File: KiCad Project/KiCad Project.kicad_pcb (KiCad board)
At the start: 4 copper layers, 69 parts, among them J1 XT30PW-M, J2 USB_C_Receptacle_USB2.0_16P, J3 PYRO, J4 PYRO ARM, J5 SWD, J6 Micro_SD_Card, Q1 GSFC02A05, Q2 FDMC7692, U1 STM32F103C8T6, U2 ICM-42670-P, U3 BME280, U4 AT25SF041B-SSHD-T, U5 PESD3V3S4UD,115, U6 AP63203WU, U7 ESD122DMXR, U8 AZ1117CH2-3.3, U9 ESD122DMXR, Y1 ECS-2520MV-160-CN-TR

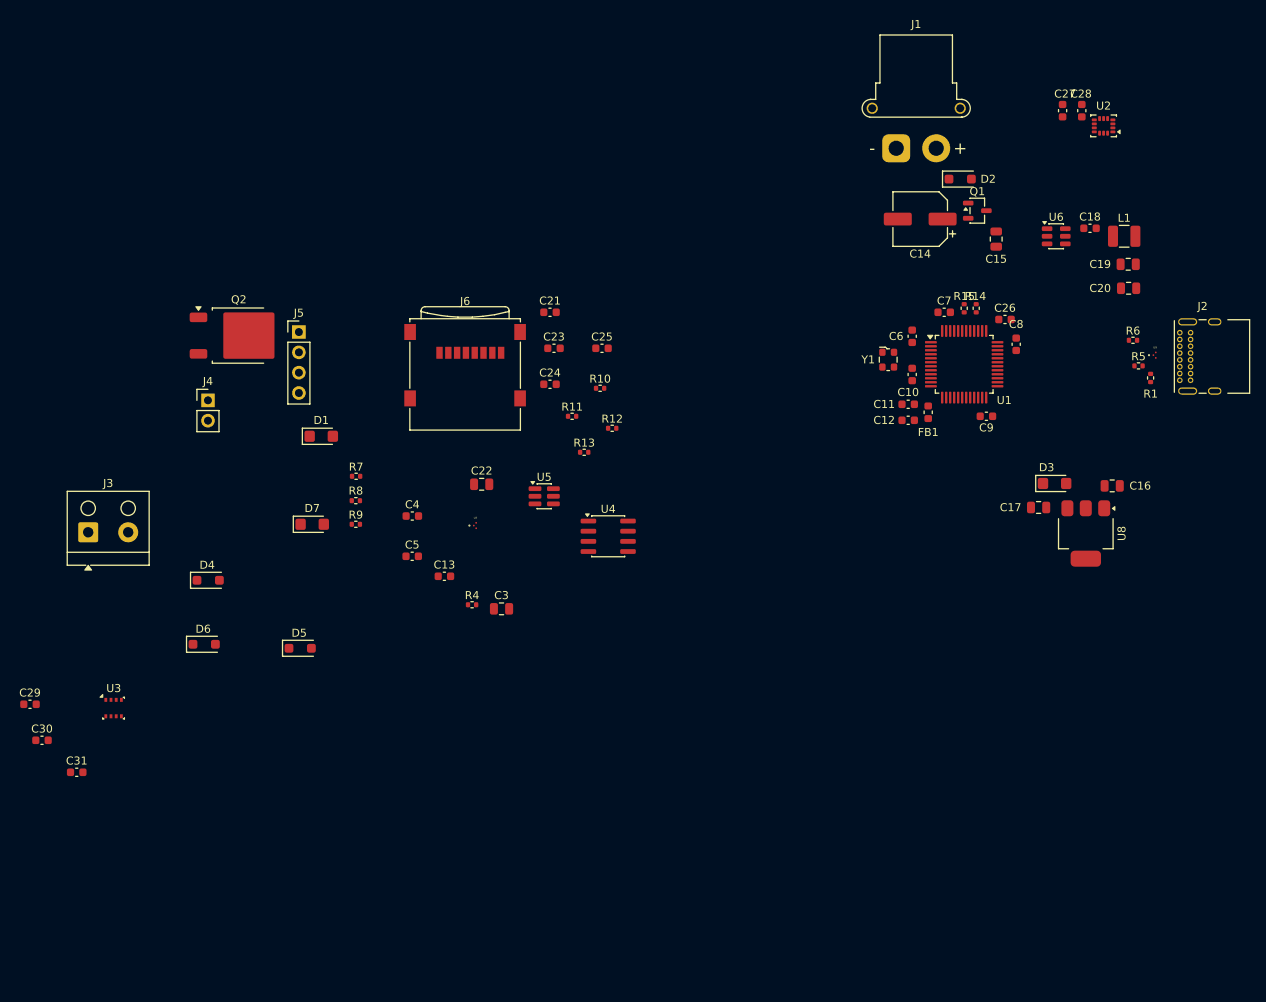
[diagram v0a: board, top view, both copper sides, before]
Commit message: Updated layout, documentation and schematic. Component placement finished.
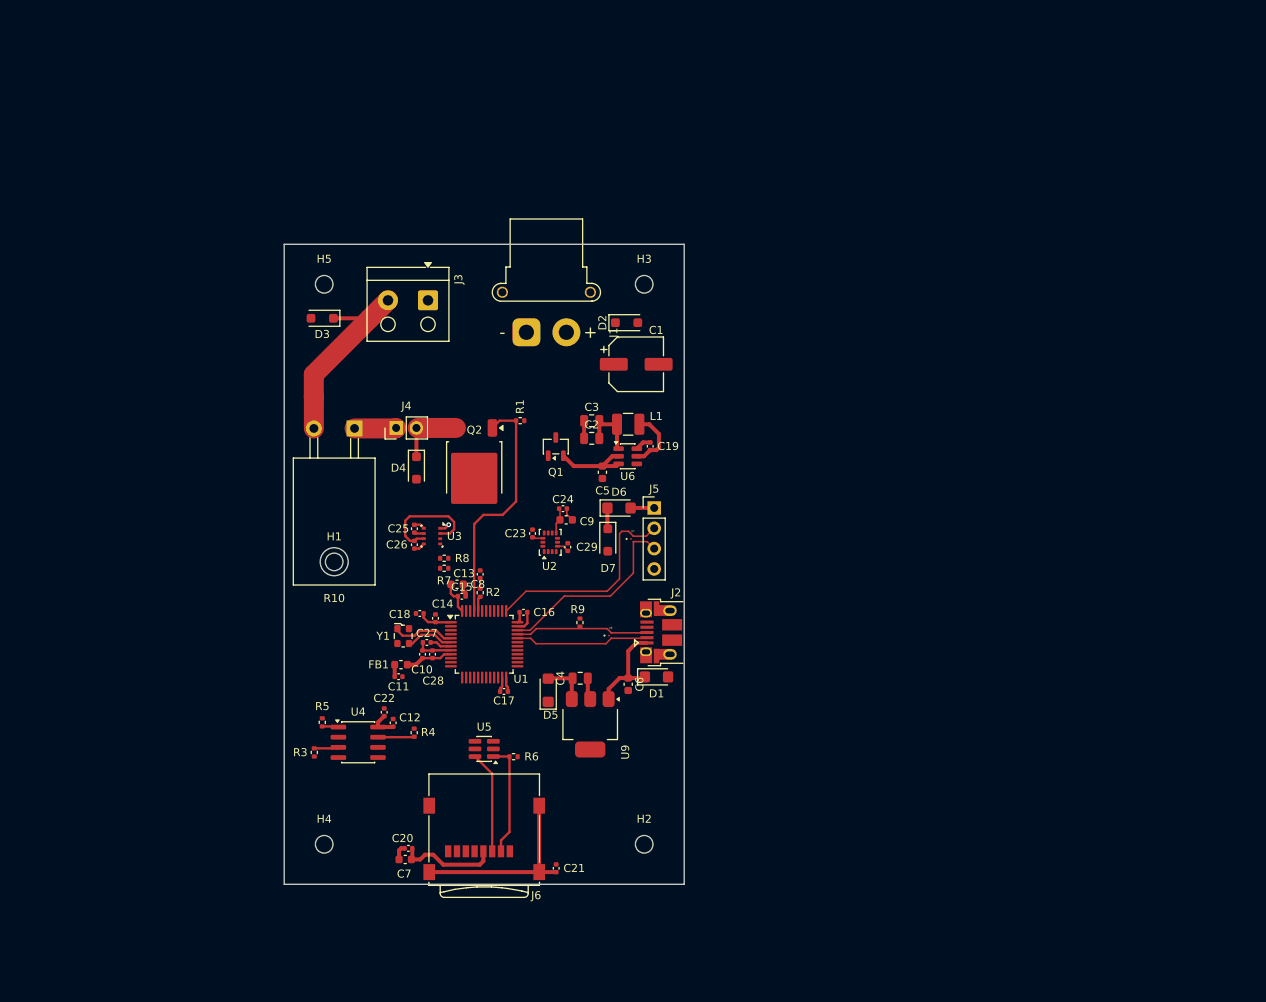
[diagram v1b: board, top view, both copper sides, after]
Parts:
- removed the R5 at (206.8, 65.2)
- removed the R6 at (206.1, 62.0)
- removed the R7 at (109.0, 79.0)
- removed the R8 at (109.0, 82.0)
- added H1: MountingHole, MountingHole:MountingHole_2.2mm_M2, F.Cu at (106.2, 89.7)
- added H2: MountingHole, MountingHole:MountingHole_2.2mm_M2, F.Cu at (145.0, 125.0)
- added H3: MountingHole, MountingHole:MountingHole_2.2mm_M2, F.Cu at (145.0, 55.0)
- added H4: MountingHole, MountingHole:MountingHole_2.2mm_M2, F.Cu at (105.0, 125.0)
- added H5: MountingHole, MountingHole:MountingHole_2.2mm_M2, F.Cu at (105.0, 55.0)
- added R10: 2R, Package_TO_SOT_THT:TO-220-2_Horizontal_TabDown, F.Cu at (108.8, 73.0)
- C10: renamed from C11; footprint Capacitor_SMD:C_0603_1608Metric -> Capacitor_SMD:C_0402_1005Metric
- C11: renamed from C12; footprint Capacitor_SMD:C_0603_1608Metric -> Capacitor_SMD:C_0402_1005Metric
- C12: renamed from C24; footprint Capacitor_SMD:C_0603_1608Metric -> Capacitor_SMD:C_0402_1005Metric
- C13: renamed from C5; footprint Capacitor_SMD:C_0603_1608Metric -> Capacitor_SMD:C_0402_1005Metric
- C14: renamed from C6; footprint Capacitor_SMD:C_0603_1608Metric -> Capacitor_SMD:C_0402_1005Metric
- C15: renamed from C7; footprint Capacitor_SMD:C_0603_1608Metric -> Capacitor_SMD:C_0402_1005Metric
- C16: renamed from C8; footprint Capacitor_SMD:C_0603_1608Metric -> Capacitor_SMD:C_0402_1005Metric
- C17: renamed from C9; footprint Capacitor_SMD:C_0603_1608Metric -> Capacitor_SMD:C_0402_1005Metric
- C18: renamed from C13; footprint Capacitor_SMD:C_0603_1608Metric -> Capacitor_SMD:C_0402_1005Metric
- C19: renamed from C18; footprint Capacitor_SMD:C_0603_1608Metric -> Capacitor_SMD:C_0402_1005Metric
- C20: renamed from C21; footprint Capacitor_SMD:C_0603_1608Metric -> Capacitor_SMD:C_0402_1005Metric
- C21: renamed from C23; footprint Capacitor_SMD:C_0603_1608Metric -> Capacitor_SMD:C_0402_1005Metric
- C22: renamed from C25; footprint Capacitor_SMD:C_0603_1608Metric -> Capacitor_SMD:C_0402_1005Metric
- C23: renamed from C26; footprint Capacitor_SMD:C_0603_1608Metric -> Capacitor_SMD:C_0402_1005Metric
- C24: renamed from C28; footprint Capacitor_SMD:C_0603_1608Metric -> Capacitor_SMD:C_0402_1005Metric
- C25: renamed from C30; footprint Capacitor_SMD:C_0603_1608Metric -> Capacitor_SMD:C_0402_1005Metric
- C26: renamed from C31; footprint Capacitor_SMD:C_0603_1608Metric -> Capacitor_SMD:C_0402_1005Metric
- C27: renamed from C4; footprint Capacitor_SMD:C_0603_1608Metric -> Capacitor_SMD:C_0402_1005Metric
- C28: renamed from C10; footprint Capacitor_SMD:C_0603_1608Metric -> Capacitor_SMD:C_0402_1005Metric
- C29: footprint Capacitor_SMD:C_0603_1608Metric -> Capacitor_SMD:C_0402_1005Metric
- C5: renamed from C15; footprint Capacitor_SMD:C_0805_2012Metric -> Capacitor_SMD:C_0603_1608Metric
- C6: renamed from C16; footprint Capacitor_SMD:C_0805_2012Metric -> Capacitor_SMD:C_0603_1608Metric
- C7: renamed from C22; footprint Capacitor_SMD:C_0805_2012Metric -> Capacitor_SMD:C_0603_1608Metric
- C8: renamed from C3; footprint Capacitor_SMD:C_0805_2012Metric -> Capacitor_SMD:C_0603_1608Metric
- J2: value USB_C_Receptacle_USB2.0_16P -> USB_B_Micro; footprint Connector_USB:USB_C_Receptacle_GCT_USB4085 -> Connector_USB:USB_Micro-B_Amphenol_10103594-0001LF_Horizontal
- moved U2 86.6 mm to (133.2, 87.2), turned to 90 degrees
- moved C24 81.7 mm to (134.8, 83.0), turned to 0 degrees
- moved C9 80.4 mm to (135.2, 84.5), turned to 0 degrees
- moved R9 77.6 mm to (137.0, 97.3)
- moved U8 76.6 mm to (140.7, 98.9)
- moved R7 74.0 mm to (120.0, 90.5), turned to 0 degrees
- moved FB1 73.1 mm to (114.6, 102.5), turned to 180 degrees
- moved R8 72.1 mm to (120.0, 89.2), turned to 0 degrees
- moved J2 72.1 mm to (147.1, 98.5)
- moved C11 71.3 mm to (114.3, 104.0)
- moved C2 70.5 mm to (138.4, 74.3)
- moved C16 70.1 mm to (129.9, 96.0), turned to 0 degrees
- moved C29 70.0 mm to (135.4, 87.8), turned to 90 degrees
- moved C15 70.0 mm to (122.2, 94.0)
- moved Y1 69.8 mm to (114.9, 99.0)
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- renumbered C14 to C1, C19 to C2, C20 to C3, C17 to C4, C27 to C9, D4 to D3, D6 to D4, D3 to D5, D7 to D6, D5 to D7, R9 to R1, R4 to R2, R11 to R3, R12 to R4, R13 to R5, R10 to R6, R14 to R7, R15 to R8, R1 to R9, U9 to U8, U8 to U9
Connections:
- C1 pad 1: +7.5V -> Net-(D2-K)
- D2 pad 1: +7.5V -> Net-(D2-K)
- D3 pad 1: Net-(D4-K) (its old number) -> Net-(D3-K)
- D4 pad 2: Net-(D4-K) (its old number) -> GND
- J3 pad 2: Net-(D4-K) (its old number) -> Net-(D3-K)
- J4 pad 1: Net-(D4-K) (its old number) -> Net-(J4-Pin_1)
- J5 pad 2: STM_SWDIO -> STM_SWCLK
- J5 pad 3: STM_SWCLK -> STM_SWDIO
- Q1 pad 2: +7.5V -> +BATT
- Q1 pad 3: +BATT -> Net-(D2-K)
- U5 pad 4: STM_MOSI -> STM_MISO
- U5 pad 6: STM_MISO -> STM_MOSI
- U8 pad 2: STM_USB_D+ -> STM_USB_D-
- U8 pad 3: STM_USB_D- -> STM_USB_D+
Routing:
- net +3.3V: track 0.00 -> 61.3 mm
- net PYRO_GATE: track 0.00 -> 30.7 mm
- net STM_SWCLK: track 0.00 -> 26.6 mm
- net GND: track 0.00 -> 24.7 mm, vias 0 -> 1
- net Net-(D3-K): track 0.00 -> 24.4 mm
- net STM_SWDIO: track 0.00 -> 24.3 mm
- net Net-(J6-SHIELD): track 0.00 -> 24.2 mm
- net STM_USB_D+: track 0.00 -> 17.5 mm
- net STM_USB_D-: track 0.00 -> 17.4 mm
- net ~{CS}_SD: track 0.00 -> 14.3 mm
- net STM_MOSI: track 0.00 -> 12.9 mm
- net VBUS: track 0.00 -> 12.6 mm
- net +BATT: track 0.00 -> 10.1 mm
- net Net-(D4-K): track 0.00 -> 8.38 mm
- net Net-(U6-SW): track 0.00 -> 7.88 mm
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- added copper zone on In2.Cu, net +3.3V
- added copper zone on In1.Cu, net GND
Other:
- board outline added: 50 x 80 mm

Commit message: PCB update
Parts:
- J1: value XT30PW-M -> BATT XT30; footprint Connector_AMASS:AMASS_XT30PW-F_1x02_P2.50mm_Horizontal -> Connector_AMASS:AMASS_XT30PW-M_1x02_P2.50mm_Horizontal
- moved C25 70.4 mm to (186.4, 79.3)
- moved C26 70.4 mm to (186.4, 81.3)
- moved U3 70.4 mm to (188.6, 80.2)
- moved C12 65.3 mm to (178.1, 120.1)
- moved C20 65.3 mm to (180.0, 135.8)
- moved C21 65.3 mm to (198.5, 138.3)
- moved C22 65.3 mm to (177.0, 118.8)
- moved C7 65.3 mm to (179.6, 137.2)
- moved J6 65.3 mm to (189.5, 134.6)
- moved R4 65.3 mm to (180.8, 121.3)
- moved R6 65.3 mm to (193.2, 124.3)
- moved U4 65.3 mm to (173.8, 122.5)
- moved U5 65.3 mm to (189.5, 123.4)
- moved R3 65.3 mm to (168.3, 123.8)
- moved R5 65.3 mm to (169.3, 120.1)
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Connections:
- C1 pad 1: Net-(D2-K) -> +7.5V
- D2 pad 1: Net-(D2-K) -> +7.5V
- J1 pad 1: (no net) -> GND
- J1 pad 2: (no net) -> +7.5V
- Q1 pad 3: Net-(D2-K) -> +7.5V
- U1 pad 39: IMU_INT1 -> IMU_INT2
- U1 pad 40: IMU_INT2 -> IMU_FSYNC
- U1 pad 41: IMU_FSYNC -> IMU_INT1
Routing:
- net GND: track 24.7 -> 91.0 mm, vias 1 -> 27
- net +7.5V: track 0.00 -> 45.4 mm
- net IMU_INT2: track 0.00 -> 29.1 mm
- net Net-(J6-SHIELD): track 24.2 -> 0.00 mm
- net IMU_FSYNC: track 0.00 -> 17.0 mm
- net ~{CS}_SD: track 14.3 -> 0.00 mm
- net STM_MOSI: track 12.9 -> 0.00 mm
- net IMU_INT1: track 0.00 -> 11.6 mm
- net +3.3V: track 61.3 -> 50.5 mm, vias 0 -> 13
- net STM_SCL: track 0.00 -> 7.44 mm, vias 0 -> 1
- net STM_SDA: track 0.00 -> 5.50 mm, vias 0 -> 1
- net ~{HOLD}_FLASH: track 4.55 -> 0.00 mm
- net PYRO_GATE: track 30.7 -> 35.1 mm
- net ~{WP}_FLASH: track 3.22 -> 0.00 mm
- net Net-(D3-K): track 24.4 -> 21.4 mm
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
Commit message: finished pcb
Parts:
- moved U5 79.3 mm to (110.4, 118.5), turned to 0 degrees
- moved U3 71.8 mm to (117.3, 88.3), turned to 90 degrees
- moved R4 71.5 mm to (114.3, 95.0)
- moved C22 70.2 mm to (111.9, 92.4)
- moved U4 70.2 mm to (108.7, 96.1)
- moved C12 70.2 mm to (113.0, 93.7)
- moved R5 70.2 mm to (104.2, 93.7)
- moved R3 69.4 mm to (104.2, 97.3)
- moved J6 68.2 mm to (122.1, 123.8)
- moved C21 67.7 mm to (131.6, 128.0), turned to 0 degrees
- moved C25 67.6 mm to (119.5, 89.1), turned to 90 degrees
- moved C26 67.2 mm to (119.5, 87.2), turned to 90 degrees
- moved R6 62.4 mm to (130.9, 121.9), turned to 90 degrees
- moved C20 49.4 mm to (131.6, 125.9), turned to 0 degrees
- moved C7 49.4 mm to (131.9, 124.6), turned to 0 degrees
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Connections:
- U1 pad 10: ~{CS}_SD -> ~{WP}_FLASH
- U1 pad 11: ~{WP}_FLASH -> ~{CS}_FLASH
- U1 pad 13: ~{CS}_FLASH -> unconnected-(U1-PA3-Pad13)
- U1 pad 18: unconnected-(U1-PB0-Pad18) -> ~{CS}_SD
- U1 pad 39: IMU_INT2 -> IMU_FSYNC
- U1 pad 40: IMU_FSYNC -> IMU_INT1
- U1 pad 41: IMU_INT1 -> IMU_INT2
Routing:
- net STM_MISO: track 0.00 -> 68.1 mm, vias 0 -> 4
- net STM_SCK: track 0.00 -> 65.1 mm, vias 0 -> 4
- net STM_MOSI: track 0.00 -> 61.4 mm, vias 0 -> 4
- net +3.3V: track 50.5 -> 104.1 mm, vias 13 -> 21
- net ~{CS}_SD: track 0.00 -> 46.1 mm, vias 0 -> 2
- net ~{WP}_FLASH: track 0.00 -> 36.8 mm, vias 0 -> 2
- net STM_SDA: track 5.50 -> 40.3 mm, vias 1 -> 0
- net ~{CS}_FLASH: track 0.00 -> 33.5 mm, vias 0 -> 2
- net STM_SCL: track 7.44 -> 40.8 mm, vias 1 -> 0
- net Net-(J6-SHIELD): track 0.00 -> 33.2 mm, vias 0 -> 4
- net GND: track 91.0 -> 116.3 mm, vias 27 -> 38
- net ~{HOLD}_FLASH: track 0.00 -> 23.7 mm, vias 0 -> 2
- net IMU_INT2: track 29.1 -> 17.5 mm, vias 0 -> 2
- net STM_SWCLK: track 25.5 -> 17.0 mm
- net STM_SWDIO: track 23.1 -> 18.8 mm
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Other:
- board text added: "+"
- board text added: "-"
- board text added: "CLK"
- board text added: "Edward Sicoe"
- board text added: "IO"
- board text added: "STMRocket 1"
- board text added: "U7"
- board text added: "https://github.com/esicoe/STMRocket"
